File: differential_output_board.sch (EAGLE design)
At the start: 26 parts, among them IC1 TJA1057

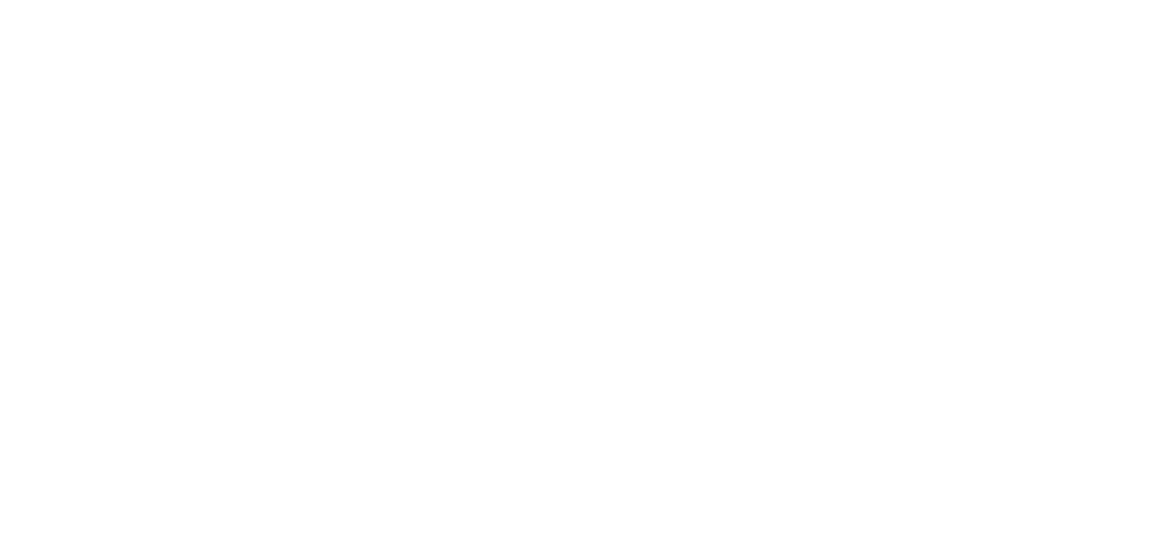
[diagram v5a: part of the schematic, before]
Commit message: added footprints for termination resistors on output connection board
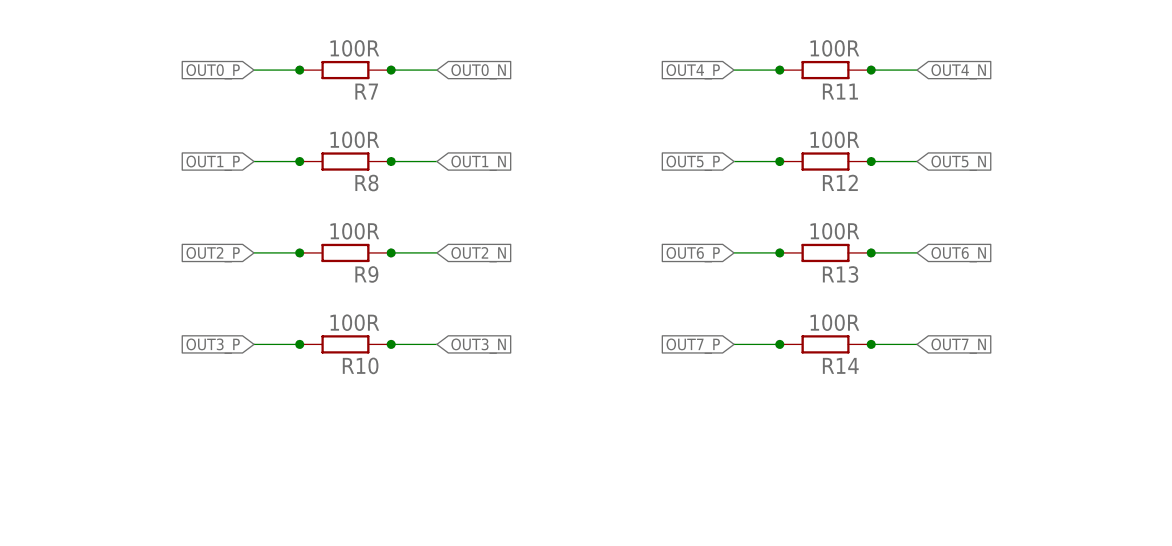
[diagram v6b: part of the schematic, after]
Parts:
- added R10, R11, R12, R13, R14, R7, R8, R9: 100R, rcl:R-EU_M1206
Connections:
- net OUT0_N: now also R7.1
- net OUT0_P: now also R7.2
- net OUT1_N: now also R8.1
- net OUT1_P: now also R8.2
- net OUT2_N: now also R9.1
- net OUT2_P: now also R9.2
- net OUT3_N: now also R10.1
- net OUT3_P: now also R10.2
- net OUT4_N: now also R11.1
- net OUT4_P: now also R11.2
- net OUT5_N: now also R12.1
- net OUT5_P: now also R12.2
- net OUT6_N: now also R13.1
- net OUT6_P: now also R13.2
- net OUT7_N: now also R14.1
- net OUT7_P: now also R14.2

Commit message: rev2 of differential output board (fix capacitor footprint)
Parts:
- C3: device rcl:CPOL-EUCT6032 -> rcl:CPOL-EUSMCD
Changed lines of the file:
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@@
 </part>
 <part name="GND5" library="supply1" library_urn="urn:adsk.eagle:library:371" deviceset="GND" device=""/>
-<part name="C3" library="rcl" library_urn="urn:adsk.eagle:library:334" deviceset="CPOL-EU" device="CT6032" package3d_urn="urn:adsk.eagle:package:23305/2" value="47µF">
+<part name="C3" library="rcl" library_urn="urn:adsk.eagle:library:334" deviceset="CPOL-EU" device="SMCD" package3d_urn="urn:adsk.eagle:package:25923/1" value="47µF">
 <spice>
 <pinmapping spiceprefix="C">
